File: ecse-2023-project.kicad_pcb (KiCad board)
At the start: 2 copper layers, 57.2 x 62.9 mm, 11 parts, among them J1 Screw_Terminal_01x02, J2 Screw_Terminal_01x02, J3 Screw_Terminal_01x02, J4 Screw_Terminal_01x03, J5 Conn_01x03_Female, Q1 IRF740, Q2 IRF740, U1 ESP32_DevKit_V1_DOIT

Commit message: replaced screw terminal with barrel jack for the power in port. changed label from 12v to power in. changed pin order for temp port to match label
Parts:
- J1: value Screw_Terminal_01x02 -> Barrel_Jack; footprint TerminalBlock_Phoenix:TerminalBlock_Phoenix_MKDS-1,5-2_1x02_P5.00mm_Horizontal -> Connector_BarrelJack:BarrelJack_Horizontal
- moved J1 8.49 mm to (114.7, 93.7), turned to 180 degrees
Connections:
- J4 pad 1: Net-(J4-Pad1) -> Net-(J5-Pad3)
- J4 pad 2: Net-(J4-Pad2) -> Net-(R3-Pad2)
- J5 pad 3: Net-(J4-Pad2) -> Net-(J5-Pad3)
- R3 pad 1: Net-(J4-Pad2) -> Net-(J5-Pad3)
- R3 pad 2: Net-(J4-Pad1) -> Net-(R3-Pad2)
- U1 pad 15: Net-(J4-Pad2) -> Net-(J5-Pad3)
- U1 pad 20: Net-(J4-Pad1) -> Net-(R3-Pad2)
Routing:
- net Net-(J4-Pad2): track 88.0 -> 0.00 mm
- net Net-(J5-Pad3): track 0.00 -> 85.5 mm
- net Net-(R3-Pad2): track 0.00 -> 54.2 mm
- net Net-(J4-Pad1): track 48.2 -> 0.00 mm
- net Net-(J1-Pad2): track 129.1 -> 142.3 mm
- net Net-(J1-Pad1): track 45.3 -> 47.3 mm
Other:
- board text added: "POWER IN"
- board text removed: "12v"

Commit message: added a buck to the pcb so that that prower port can power the esp
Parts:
- added J6: Conn_02x02_Counter_Clockwise, Library:SRT_MPT1584EN_Module, F.Cu at (86.5, 78.5)
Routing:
- net Net-(J4-Pin_3): track 142.3 -> 185.9 mm
- net Net-(J2-Pin_1): track 47.3 -> 85.6 mm
- net Net-(J4-Pin_1): track 85.5 -> 104.1 mm

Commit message: added optional buck converter for esp
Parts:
- added J7: Conn_01x02_Pin, Connector_PinHeader_2.54mm:PinHeader_1x02_P2.54mm_Vertical, F.Cu at (107.0, 93.5)
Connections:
- J6 pad 1: Net-(J4-Pin_3) -> Net-(J6-Pin_1)
- J6 pad 2: Net-(J2-Pin_1) -> Net-(J4-Pin_3)
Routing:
- net Net-(J2-Pin_1): track 85.6 -> 55.0 mm
- net Net-(J6-Pin_1): track 0.00 -> 18.6 mm
- net Net-(J4-Pin_3): track 185.9 -> 184.8 mm

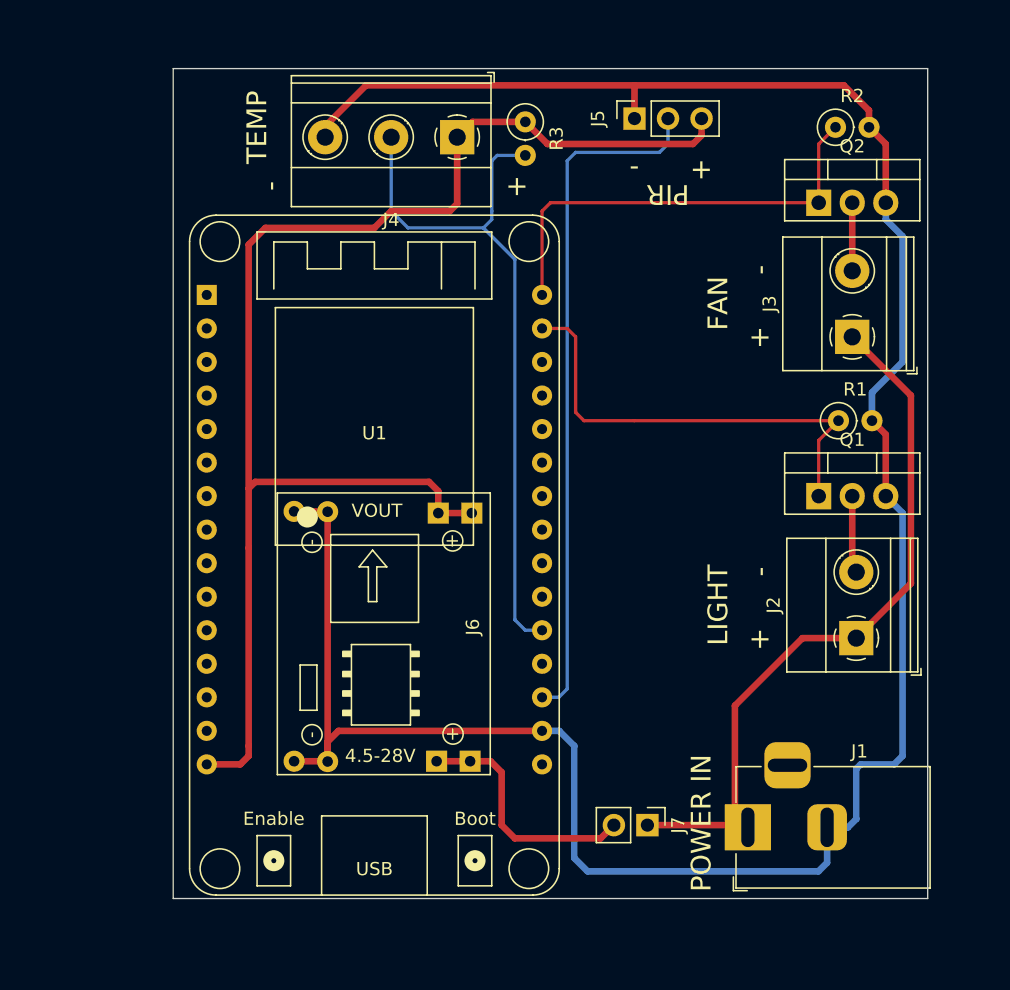
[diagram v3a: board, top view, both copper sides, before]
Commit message: added a gnd component to the sch and a gnd plain to the pcb
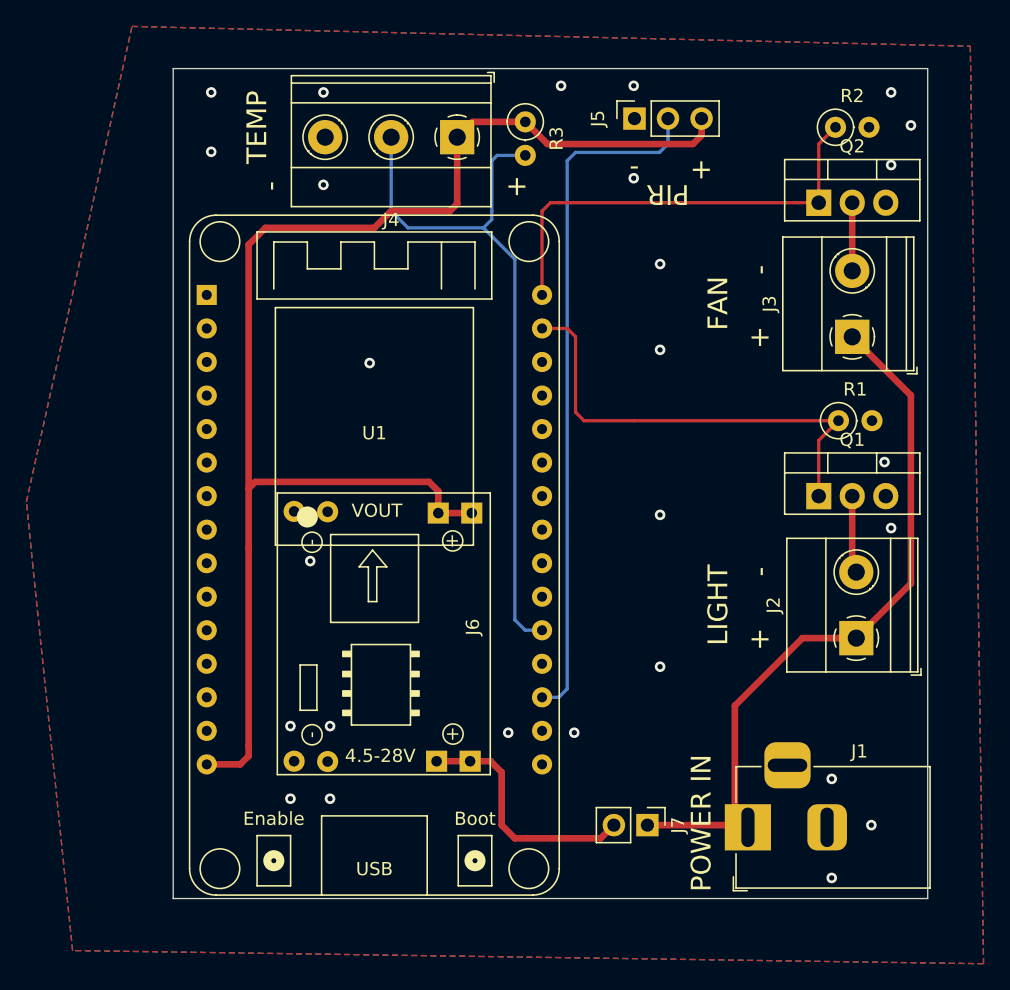
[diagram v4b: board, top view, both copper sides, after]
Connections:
- net Net-(J4-Pin_3) renamed GND
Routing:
- net GND: track 184.8 -> 0.00 mm, vias 0 -> 27
- added copper zone on B.Cu, net GND
- added copper zone on F.Cu, net GND
